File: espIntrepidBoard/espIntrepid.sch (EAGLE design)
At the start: 22 parts, among them Q1 TRANS_NPN, Q7 TRANS_NPN, U1 ESP32DEV_38, U2 MOSFET_P, U3 LTV-847, U4 PS2801C-1, U5 SN65HVD232DSOIC8

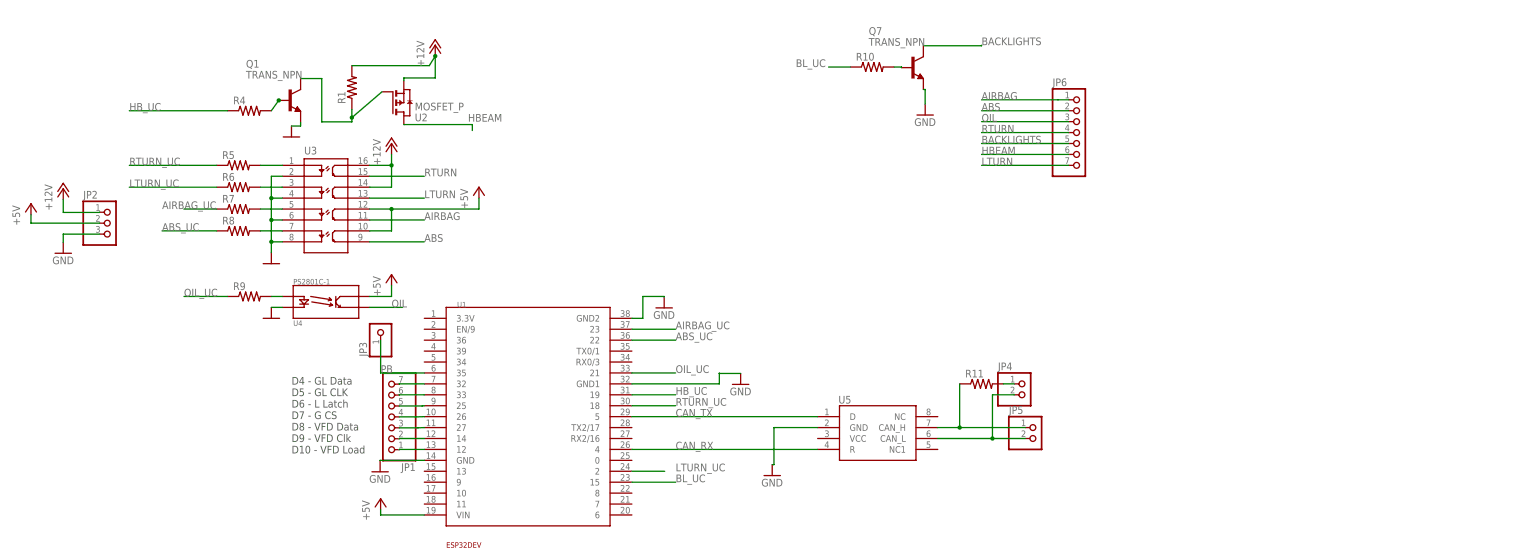
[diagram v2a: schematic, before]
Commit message: Created esp32 arduino program
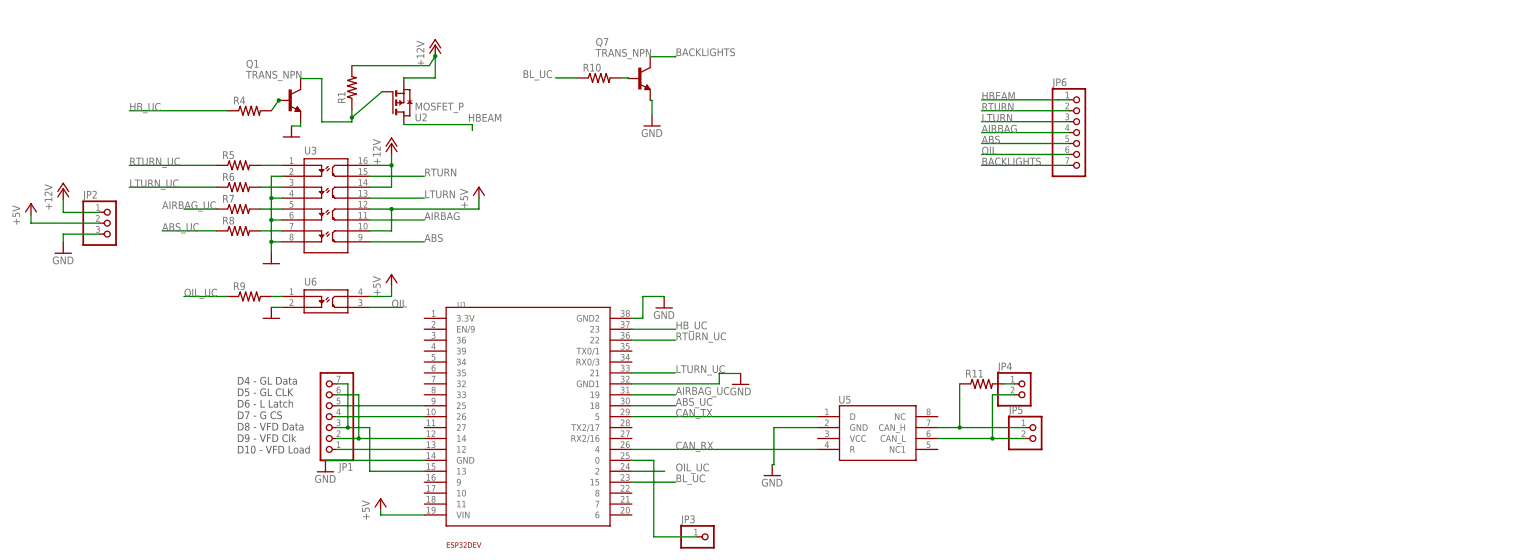
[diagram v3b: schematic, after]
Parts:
- removed U4: PS2801C-1, SureFireParts 6.0:PS2801C-1
- added U6: LTV-817, DR:LTV-817
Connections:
- removed net N$4 (its old number): JP1.7, U1.32
- removed net N$5 (its old number): JP1.6, U1.33
- removed net N$9: JP1.2, U1.14
- removed net PB: JP3.1, U1.35
- new net N$16: R9.2, U6.P$1
- new net N$7: JP1.3, JP1.7, U1.13
- net +5V: now also U6.P$4; no longer U4.4
- net ABS: now also JP6.5; no longer JP6.2
- net ABS_UC: now also U1.18; no longer U1.22
- net AIRBAG: now also JP6.4; no longer JP6.1
- net AIRBAG_UC: now also U1.19; no longer U1.23
- net BACKLIGHTS: now also JP6.7; no longer JP6.5
- net GND: now also U6.P$2; no longer U4.2
- net HBEAM: now also JP6.1; no longer JP6.6
- net HB_UC: now also U1.23; no longer U1.19
- net LTURN: now also JP6.3; no longer JP6.7
- net LTURN_UC: now also U1.21; no longer U1.2
- net N$17: now also JP3.1, U1.0; no longer R9.2, U4.1
- net N$8: now also JP1.2, JP1.6, U1.14; no longer JP1.3, U1.27
- net OIL: now also JP6.6, U6.P$3; no longer JP6.3, U4.3
- net OIL_UC: now also U1.2; no longer U1.21
- net RTURN: now also JP6.2; no longer JP6.4
- net RTURN_UC: now also U1.22; no longer U1.18
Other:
- moved on the sheet: JP1, JP3, Q7, R10

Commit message: Made improvements to board (small stuff)
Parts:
- added JP7: (no value), pinhead:PINHD-1X2
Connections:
- net +12V: now also JP7.1
- net GND: now also JP7.2
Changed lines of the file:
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@@
 <part name="P+7" library="supply1" deviceset="+5V" device=""/>
 <part name="U6" library="DR" deviceset="LTV-817" device=""/>
+<part name="JP7" library="pinhead" library_urn="urn:adsk.eagle:library:325" deviceset="PINHD-1X2" device="" package3d_urn="urn:adsk.eagle:package:22435/2"/>
+<part name="P+8" library="supply1" deviceset="+12V" device=""/>
+<part name="GND10" library="supply1" deviceset="GND" device=""/>
 </parts>
 <sheets>
@@
 <attribute name="VALUE" x="65.92" y="17.66" size="1.778" layer="96"/>
 </instance>
-<instance part="GND7" gate="1" x="164.98" y="40.52" smashed="yes">
-<attribute name="VALUE" x="162.44" y="37.98" size="1.778" layer="96"/>
+<instance part="GND7" gate="1" x="167.64" y="38.1" smashed="yes">
+<attribute name="VALUE" x="165.1" y="35.56" size="1.778" layer="96"/>
 </instance>
 <instance part="Q7" gate="G$1" x="138.88" y="111.62" smashed="yes">
@@
 <attribute name="NAME" x="63.5" y="63.5" size="1.778" layer="95"/>
 </instance>
+<instance part="JP7" gate="G$1" x="233.68" y="20.32" smashed="yes">
+<attribute name="NAME" x="227.33" y="26.035" size="1.778" layer="95"/>
+<attribute name="VALUE" x="227.33" y="15.24" size="1.778" layer="96"/>
+</instance>
+<instance part="P+8" gate="1" x="220.98" y="22.86" smashed="yes">
+<attribute name="VALUE" x="218.44" y="17.78" size="1.778" layer="96" rot="R90"/>
+</instance>
+<instance part="GND10" gate="1" x="220.98" y="12.7" smashed="yes"/>
 </instances>
 <busses>
@@
 <wire x1="91.44" y1="22.86" x2="68.46" y2="22.86" width="0.1524" layer="91"/>
 <wire x1="68.46" y1="22.86" x2="68.46" y2="22.74" width="0.1524" layer="91"/>
-</segment>
-<segment>
-<pinref part="U1" gate="G$1" pin="GND1"/>
-<wire x1="139.7" y1="40.64" x2="160.02" y2="40.64" width="0.1524" layer="91"/>
-<wire x1="160.02" y1="40.64" x2="160.02" y2="43.06" width="0.1524" layer="91"/>
-<pinref part="GND7" gate="1" pin="GND"/>
-<wire x1="160.02" y1="43.18" x2="160.02" y2="43.06" width="0.1524" layer="91"/>
-<wire x1="160.02" y1="43.06" x2="164.98" y2="43.06" width="0.1524" layer="91"/>
 </segment>
 <segment>
@@
 <wire x1="58.42" y1="58.42" x2="55.88" y2="58.42" width="0.1524" layer="91"/>
 </segment>
+<segment>
+<pinref part="U1" gate="G$1" pin="GND1"/>
+<wire x1="139.7" y1="40.64" x2="167.64" y2="40.64" width="0.1524" layer="91"/>
+<pinref part="GND7" gate="1" pin="GND"/>
+</segment>
+<segment>
+<pinref part="JP7" gate="G$1" pin="2"/>
+<wire x1="231.14" y1="20.32" x2="226.06" y2="20.32" width="0.1524" layer="91"/>
+<wire x1="226.06" y1="20.32" x2="226.06" y2="15.24" width="0.1524" layer="91"/>
+<pinref part="GND10" gate="1" pin="GND"/>
+<wire x1="226.06" y1="15.24" x2="220.98" y2="15.24" width="0.1524" layer="91"/>
+</segment>
 </net>
 <net name="+5V" class="0">
@@
 <junction x="83.82" y="91.44"/>
 </segment>
+<segment>
+<pinref part="P+8" gate="1" pin="+12V"/>
+<wire x1="220.98" y1="20.32" x2="223.52" y2="20.32" width="0.1524" layer="91"/>
+<wire x1="223.52" y1="20.32" x2="223.52" y2="22.86" width="0.1524" layer="91"/>
+<pinref part="JP7" gate="G$1" pin="1"/>
+<wire x1="223.52" y1="22.86" x2="231.14" y2="22.86" width="0.1524" layer="91"/>
+</segment>
 </net>

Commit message: Finished board
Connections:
- net N$7: now also JP1.6; no longer JP1.7
- net N$8: now also JP1.7; no longer JP1.6
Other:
- note added: "D4 - GL CLK D5 - GL Data D6 - L Latch D7 - G CS D8 - VFD Data D9 - VFD Clk D10 - VFD Load"
- note removed: "D4 - GL Data D5 - GL CLK D6 - L Latch D7 - G CS D8 - VFD Data D9 - VFD Clk D10 - VFD Load"
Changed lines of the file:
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@@
 <sheet>
 <plain>
-<text x="47.88" y="24.46" size="1.778" layer="97">D4 - GL Data
-D5 - GL CLK
+<text x="47.88" y="24.46" size="1.778" layer="97">D4 - GL CLK
+D5 - GL Data
 D6 - L Latch
 D7 - G CS
@@
 <segment>
 <pinref part="JP1" gate="A" pin="3"/>
-<wire x1="71.12" y1="30.48" x2="73.66" y2="30.48" width="0.1524" layer="91"/>
-<wire x1="73.66" y1="30.48" x2="73.66" y2="40.64" width="0.1524" layer="91"/>
-<pinref part="JP1" gate="A" pin="7"/>
-<wire x1="73.66" y1="40.64" x2="71.12" y2="40.64" width="0.1524" layer="91"/>
 <pinref part="U1" gate="G$1" pin="13"/>
 <wire x1="91.44" y1="20.32" x2="78.74" y2="20.32" width="0.1524" layer="91"/>
 <wire x1="78.74" y1="20.32" x2="78.74" y2="30.48" width="0.1524" layer="91"/>
-<wire x1="78.74" y1="30.48" x2="73.66" y2="30.48" width="0.1524" layer="91"/>
-<junction x="73.66" y="30.48"/>
+<wire x1="78.74" y1="30.48" x2="71.12" y2="30.48" width="0.1524" layer="91"/>
+<pinref part="JP1" gate="A" pin="6"/>
+<wire x1="71.12" y1="38.1" x2="78.74" y2="38.1" width="0.1524" layer="91"/>
+<wire x1="78.74" y1="38.1" x2="78.74" y2="30.48" width="0.1524" layer="91"/>
+<junction x="78.74" y="30.48"/>
 </segment>
 </net>
 <net name="N$8" class="0">
 <segment>
-<pinref part="JP1" gate="A" pin="6"/>
-<wire x1="71.12" y1="38.1" x2="76.2" y2="38.1" width="0.1524" layer="91"/>
-<wire x1="76.2" y1="38.1" x2="76.2" y2="27.94" width="0.1524" layer="91"/>
+<wire x1="76.2" y1="40.64" x2="76.2" y2="27.94" width="0.1524" layer="91"/>
 <pinref part="JP1" gate="A" pin="2"/>
 <wire x1="76.2" y1="27.94" x2="71.12" y2="27.94" width="0.1524" layer="91"/>
@@
 <wire x1="91.44" y1="27.94" x2="76.2" y2="27.94" width="0.1524" layer="91"/>
 <junction x="76.2" y="27.94"/>
-</segment>
-</net>
+<pinref part="JP1" gate="A" pin="7"/>
+<wire x1="71.12" y1="40.64" x2="76.2" y2="40.64" width="0.1524" layer="91"/>
+</segment>
+</net>

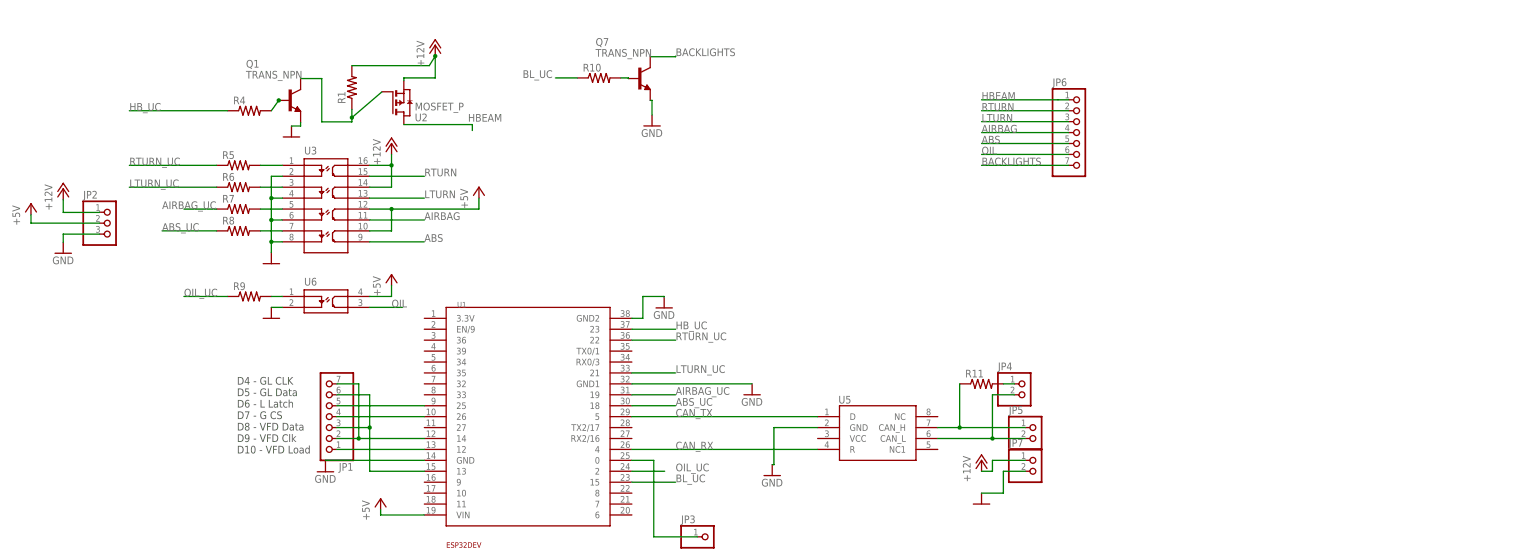
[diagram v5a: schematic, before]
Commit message: Made fixes to board, started V1.1
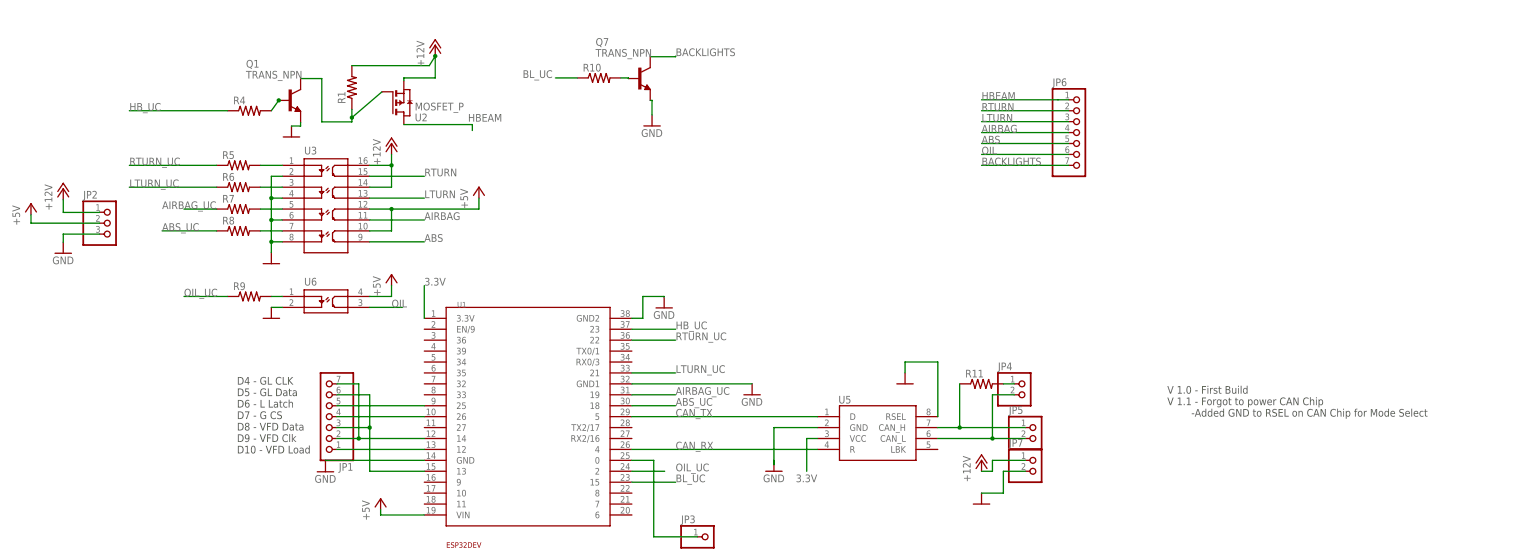
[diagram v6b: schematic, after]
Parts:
- U5: value SN65HVD232DSOIC8 -> SN65HVD233D; device DR:SN65HVD232DSOIC8 -> DR:SN65HVD233D
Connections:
- new net 3.3V: U1.3.3V, U5.VCC
- net GND: now also U5.RSEL
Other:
- note added: "V 1.0 - First Build V 1.1 - Forgot to power CAN Chip -Added GND to RSEL on CAN Chip for Mode Select"
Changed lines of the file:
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@@
 <layer number="56" name="wert" color="7" fill="1" visible="no" active="no"/>
 <layer number="57" name="tCAD" color="7" fill="1" visible="no" active="no"/>
+<layer number="88" name="SimResults" color="9" fill="1" visible="no" active="no"/>
+<layer number="89" name="SimProbes" color="9" fill="1" visible="no" active="no"/>
 <layer number="90" name="Modules" color="5" fill="1" visible="yes" active="yes"/>
 <layer number="91" name="Nets" color="2" fill="1" visible="yes" active="yes"/>
@@
 <part name="R10" library="DR" deviceset="R-US_" device="M1206"/>
 <part name="GND8" library="supply1" deviceset="GND" device=""/>
-<part name="U5" library="DR" deviceset="SN65HVD232D" device="SOIC8"/>
+<part name="U5" library="DR" deviceset="SN65HVD233D" device=""/>
 <part name="GND9" library="supply1" deviceset="GND" device=""/>
 <part name="R11" library="DR" deviceset="R-US_" device="M1206"/>
@@
 <part name="P+8" library="supply1" deviceset="+12V" device=""/>
 <part name="GND10" library="supply1" deviceset="GND" device=""/>
+<part name="GND11" library="supply1" deviceset="GND" device=""/>
 </parts>
 <sheets>
@@
 D9 - VFD Clk
 D10 - VFD Load</text>
+<text x="264.16" y="33.02" size="1.778" layer="97">V 1.0 - First Build
+V 1.1 - Forgot to power CAN Chip
+        -Added GND to RSEL on CAN Chip for Mode Select</text>
 </plain>
 <instances>
@@
 <attribute name="NAME" x="187.706" y="36.068" size="1.778" layer="95"/>
 </instance>
-<instance part="GND9" gate="1" x="172.32" y="19.32" smashed="yes">
-<attribute name="VALUE" x="169.78" y="16.78" size="1.778" layer="96"/>
+<instance part="GND9" gate="1" x="172.72" y="20.32" smashed="yes">
+<attribute name="VALUE" x="170.18" y="17.78" size="1.778" layer="96"/>
 </instance>
 <instance part="R11" gate="G$1" x="220.98" y="40.64" smashed="yes">
@@
 </instance>
 <instance part="GND10" gate="1" x="220.98" y="12.7" smashed="yes"/>
+<instance part="GND11" gate="1" x="203.2" y="40.64" smashed="yes"/>
 </instances>
 <busses>
@@
 <pinref part="GND9" gate="1" pin="GND"/>
 <wire x1="172.72" y1="30.48" x2="172.72" y2="21.86" width="0.1524" layer="91"/>
-<wire x1="172.72" y1="21.86" x2="172.32" y2="21.86" width="0.1524" layer="91"/>
+<wire x1="172.72" y1="21.86" x2="172.72" y2="22.86" width="0.1524" layer="91"/>
 </segment>
 <segment>
@@
 <wire x1="226.06" y1="15.24" x2="220.98" y2="15.24" width="0.1524" layer="91"/>
 </segment>
+<segment>
+<pinref part="U5" gate="G$1" pin="RSEL"/>
+<wire x1="210.82" y1="33.02" x2="210.82" y2="45.72" width="0.1524" layer="91"/>
+<wire x1="210.82" y1="45.72" x2="203.2" y2="45.72" width="0.1524" layer="91"/>
+<pinref part="GND11" gate="1" pin="GND"/>
+<wire x1="203.2" y1="45.72" x2="203.2" y2="43.18" width="0.1524" layer="91"/>
+</segment>
 </net>
 <net name="+5V" class="0">
@@
 </segment>
 </net>
+<net name="3.3V" class="0">
+<segment>
+<pinref part="U5" gate="G$1" pin="VCC"/>
+<wire x1="182.88" y1="27.94" x2="180.34" y2="27.94" width="0.1524" layer="91"/>
+<wire x1="180.34" y1="27.94" x2="180.34" y2="20.32" width="0.1524" layer="91"/>
+<label x="177.8" y="17.78" size="1.778" layer="95"/>
+</segment>
+<segment>
+<wire x1="91.44" y1="63.5" x2="91.44" y2="55.88" width="0.1524" layer="91"/>
+<pinref part="U1" gate="G$1" pin="3.3V"/>
+<label x="91.44" y="63.5" size="1.778" layer="95"/>
+</segment>
+</net>

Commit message: -Swapped 2 pins on board -Added reverse engg schematic
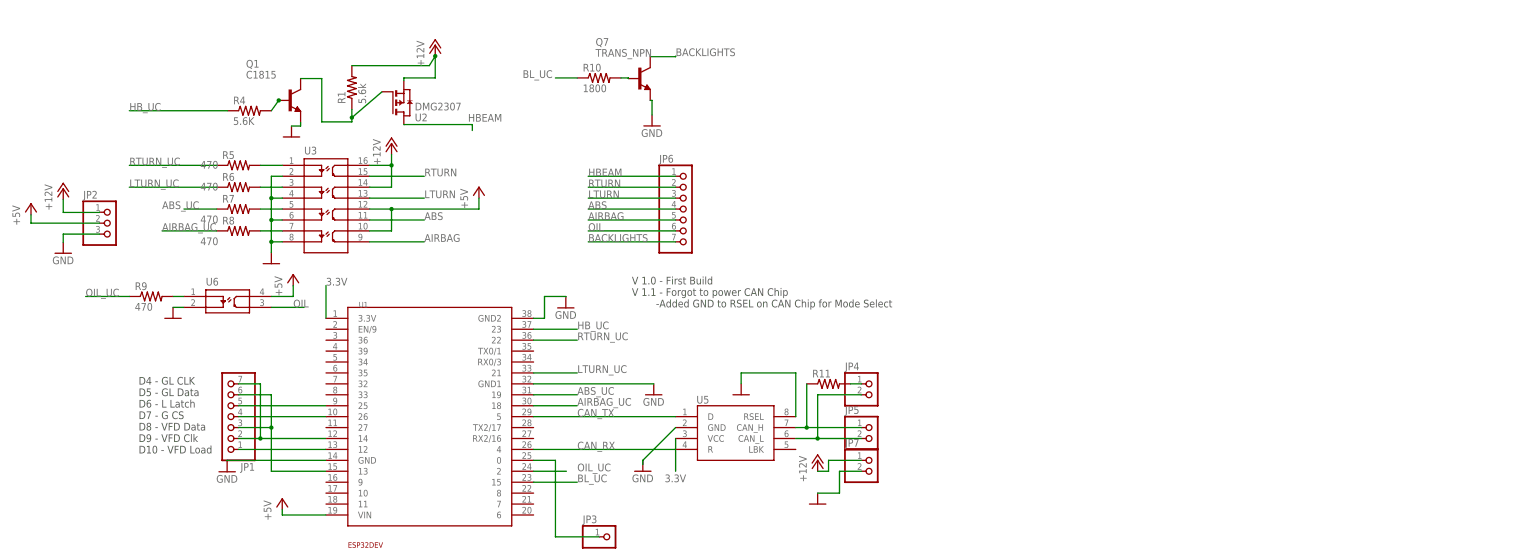
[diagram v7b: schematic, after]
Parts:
- Q1: value TRANS_NPN -> C1815
- R1: value (none) -> 5.6k
- R10: value (none) -> 1800
- R4: value (none) -> 5.6K
- R5, R6, R7, R8, R9: value (none) -> 470
- U2: value MOSFET_P -> DMG2307
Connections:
- net ABS: now also JP6.4, U3.P$11; no longer JP6.5, U3.P$9
- net ABS_UC: now also R7.1, U1.19; no longer R8.1, U1.18
- net AIRBAG: now also JP6.5, U3.P$9; no longer JP6.4, U3.P$11
- net AIRBAG_UC: now also R8.1, U1.18; no longer R7.1, U1.19
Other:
- moved on the sheet: JP1, JP3, JP4, JP5, JP6, JP7, R11, R9, U1, U5, U6
